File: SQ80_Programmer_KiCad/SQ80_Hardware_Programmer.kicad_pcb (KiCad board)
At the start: 2 copper layers, 225 x 115 mm, 58 parts, among them J1 MIDI IN, J2 MIDI OUT/THRU, SW1 ARCH_MODE, SW2 GLITCH_TRIG, U1 MUX_1, U2 MUX_2, U3 6N138, U4 ER_OLEDM0.91_1x-I2C

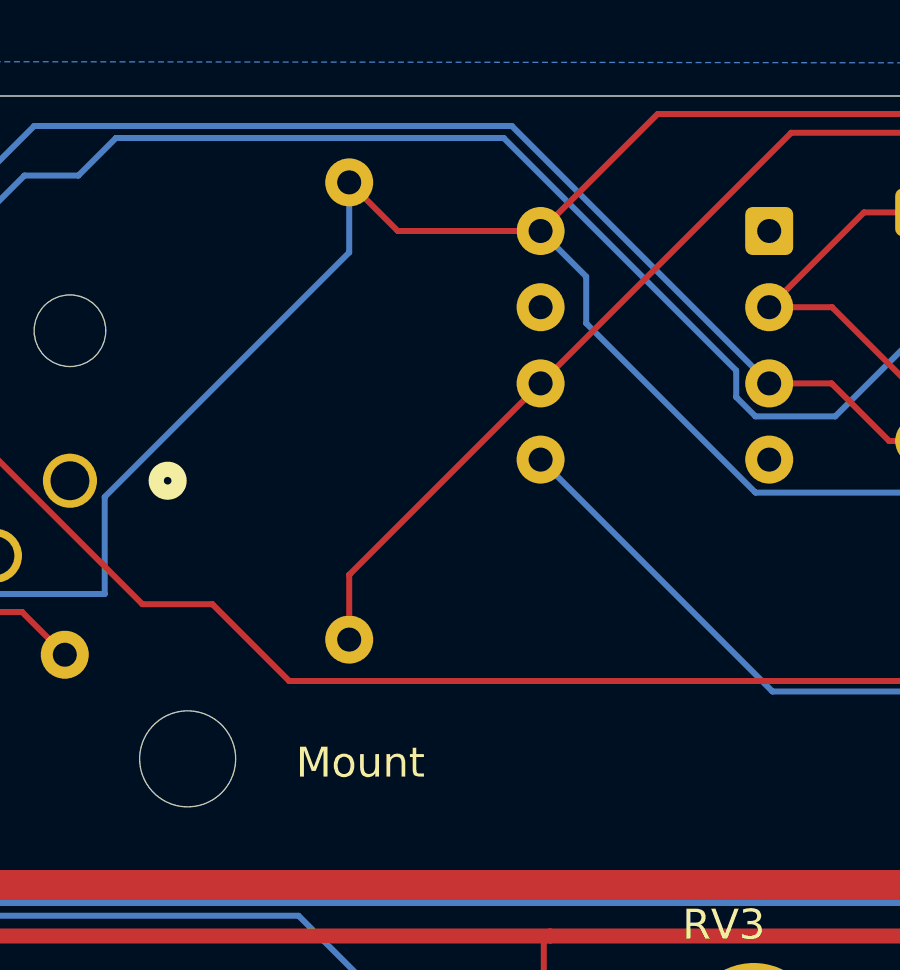
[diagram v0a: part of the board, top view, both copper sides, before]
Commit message: PCB and Readme Updates
Added functional descriptions for SW1 and SW2 in README.  Update PCB to add R5 to MIDI input section.
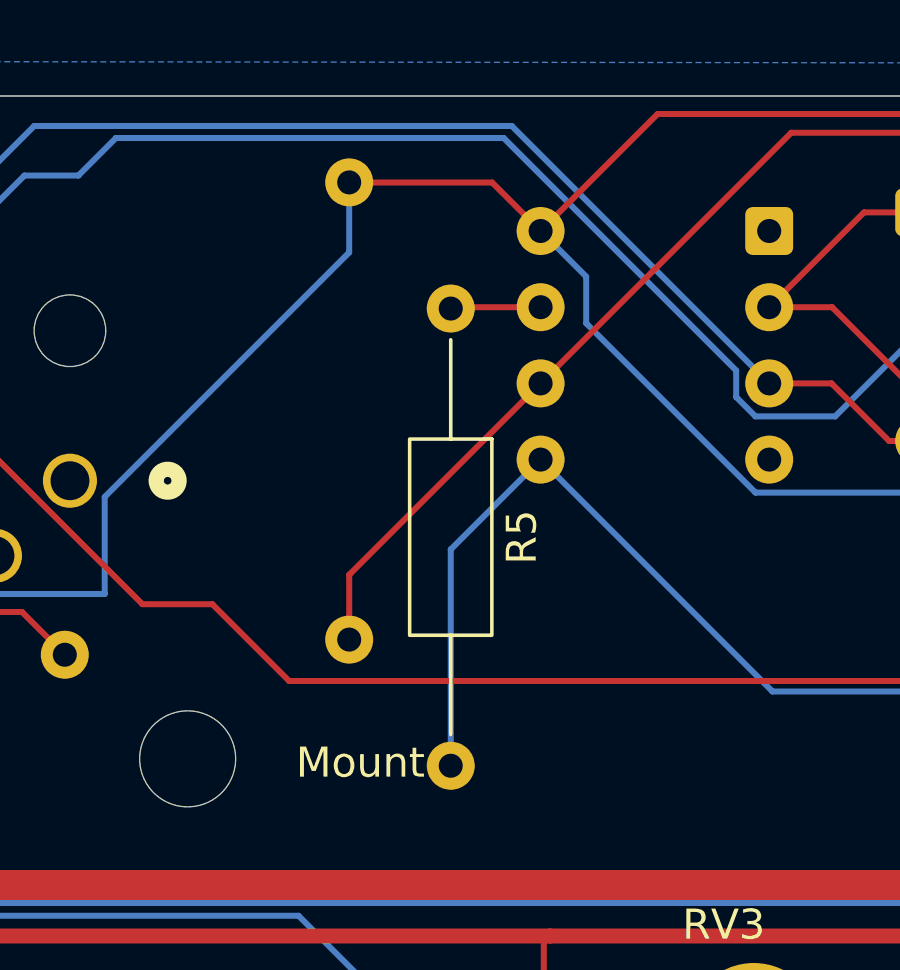
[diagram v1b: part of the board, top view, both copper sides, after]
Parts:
- added R5: 4.7k, Resistor_THT:R_Axial_DIN0207_L6.3mm_D2.5mm_P15.24mm_Horizontal, F.Cu at (96.5, 40.8)
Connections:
- U3 pad 7: unconnected-(U3-VO1-Pad7) -> Net-(U3-VO1)
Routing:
- net GND: track 1582.2 -> 1593.6 mm
- net Net-(U3-VO1): track 0.00 -> 3.01 mm
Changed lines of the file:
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@@
 		)
 	)
+	(footprint "Resistor_THT:R_Axial_DIN0207_L6.3mm_D2.5mm_P15.24mm_Horizontal"
+		(layer "F.Cu")
+		(at 96.51 40.81 -90)
+		(descr "Resistor, Axial_DIN0207 series, Axial, Horizontal, pin pitch=15.24mm, 0.25W = 1/4W, length*diameter=6.3*2.5mm^2, http://cdn-reichelt.de/documents/datenblatt/B400/1_4W%23YAG.pdf")
+		(tags "Resistor Axial_DIN0207 series Axial Horizontal pin pitch 15.24mm 0.25W = 1/4W length 6.3mm diameter 2.5mm")
+		(property "Reference" "R5"
+			(at 7.62 -2.37 90)
+			(layer "F.SilkS")
+			(effects
+				(font
+					(size 1 1)
+					(thickness 0.15)
+				)
+			)
+		)
+		(property "Value" "4.7k"
+			(at 7.62 2.37 90)
+			(layer "F.Fab")
+			(effects
+				(font
+					(size 1 1)
+					(thickness 0.15)
+				)
+			)
+		)
+		(property "Datasheet" ""
+			(at 0 0 90)
+			(layer "F.Fab")
+			(hide yes)
+			(effects
+				(font
+					(size 1.27 1.27)
+				)
+			)
+		)
+		(property "Description" "Resistor"
+			(at 0 0 90)
+			(layer "F.Fab")
+			(hide yes)
+			(effects
+				(font
+					(size 1.27 1.27)
+				)
+			)
+		)
+		(property "KiLib_Generator" "resistor/THT"
+			(at 0 0 90)
+			(layer "F.SilkS")
+			(hide yes)
+			(effects
+				(font
+					(size 1 1)
+					(thickness 0.15)
+				)
+			)
+		)
+		(property ki_fp_filters "R_*")
+		(sheetname "/")
+		(sheetfile "SQ80_Hardware_Programmer.kicad_sch")
+		(attr through_hole)
+		(duplicate_pad_numbers_are_jumpers no)
+		(fp_line
+			(start 1.04 0)
+			(end 4.35 0)
+			(stroke
+				(width 0.12)
+				(type solid)
+			)
+			(layer "F.SilkS")
+		)
+		(fp_line
+			(start 14.2 0)
+			(end 10.89 0)
+			(stroke
+				(width 0.12)
+				(type solid)
+			)
+			(layer "F.SilkS")
+		)
+		(fp_rect
+			(start 4.35 -1.37)
+			(end 10.89 1.37)
+			(stroke
+				(width 0.12)
+				(type solid)
+			)
+			(fill no)
+			(layer "F.SilkS")
+		)
+		(fp_rect
+			(start -1.05 -1.5)
+			(end 16.29 1.5)
+			(stroke
+				(width 0.05)
+				(type solid)
+			)
+			(fill no)
+			(layer "F.CrtYd")
+		)
+		(fp_line
+			(start 0 0)
+			(end 4.47 0)
+			(stroke
+				(width 0.1)
+				(type solid)
+			)
+			(layer "F.Fab")
+		)
+		(fp_line
+			(start 15.24 0)
+			(end 10.77 0)
+			(stroke
+				(width 0.1)
+				(type solid)
+			)
+			(layer "F.Fab")
+		)
+		(fp_rect
+			(start 4.47 -1.25)
+			(end 10.77 1.25)
+			(stroke
+				(width 0.1)
+				(type solid)
+			)
+			(fill no)
+			(layer "F.Fab")
+		)
+		(fp_text user "${REFERENCE}"
+			(at 7.62 0 90)
+			(layer "F.Fab")
+			(effects
+				(font
+					(size 1 1)
+					(thickness 0.15)
+				)
+			)
+		)
+		(pad "1" thru_hole circle
+			(at 0 0 270)
+			(size 1.6 1.6)
+			(drill 0.8)
+			(layers "*.Cu" "*.Mask")
+			(remove_unused_layers no)
+			(net "Net-(U3-VO1)")
+			(pintype "passive")
+		)
+		(pad "2" thru_hole circle
+			(at 15.24 0 270)
+			(size 1.6 1.6)
+			(drill 0.8)
+			(layers "*.Cu" "*.Mask")
+			(remove_unused_layers no)
+			(net "GND")
+			(pintype "passive")
+		)
+		(embedded_fonts no)
+		(model "${KICAD10_3DMODEL_DIR}/Resistor_THT.3dshapes/R_Axial_DIN0207_L6.3mm_D2.5mm_P15.24mm_Horizontal.step"
+			(offset
+				(xyz 0 0 0)
+			)
+			(scale
+				(xyz 1 1 1)
+			)
+			(rotate
+				(xyz 0 0 0)
+			)
+		)
+	)
 	(footprint "Potentiometer_THT:Potentiometer_Bourns_PTV09A-1_Single_Vertical"
 		(layer "F.Cu")
@@
 			(layers "*.Cu" "*.Mask")
 			(remove_unused_layers no)
-			(net "unconnected-(U3-VO1-Pad7)")
+			(net "Net-(U3-VO1)")
 			(pinfunction "VO1_7")
-			(pintype "passive+no_connect")
+			(pintype "passive")
 		)
 		(pad "8" thru_hole circle
@@
 	)
 	(segment
+		(start 96.51 56.05)
+		(end 96.51 48.84)
+		(width 0.2)
+		(layer "B.Cu")
+		(net "GND")
+	)
+	(segment
 		(start 239.125 106.225)
 		(end 237.8 106.225)
@@
 	)
 	(segment
+		(start 96.51 48.84)
+		(end 99.505 45.845)
+		(width 0.2)
+		(layer "B.Cu")
+		(net "GND")
+	)
+	(segment
 		(start 178.210001 56.74)
 		(end 180.750001 59.28)
@@
 	)
 	(segment
+		(start 93.13 36.61)
+		(end 93.125 36.605)
+		(width 0.2)
+		(layer "F.Cu")
+		(net "+5V")
+	)
+	(segment
 		(start 71.125 108.225)
 		(end 42.625 108.225)
@@
 	)
 	(segment
+		(start 97.89 36.61)
+		(end 93.13 36.61)
+		(width 0.2)
+		(layer "F.Cu")
+		(net "+5V")
+	)
+	(segment
 		(start 205.3 61.775)
 		(end 205.25 61.725)
@@
 	)
 	(segment
-		(start 99.505 38.225)
-		(end 94.745 38.225)
-		(width 0.2)
-		(layer "F.Cu")
-		(net "+5V")
-	)
-	(segment
 		(start 99.717857 90.058333)
 		(end 99.717857 84.817857)
@@
 	)
 	(segment
-		(start 94.745 38.225)
-		(end 93.125 36.605)
-		(width 0.2)
+		(start 185.625 61.725)
+		(end 156.925 61.725)
+		(width 0.5)
 		(layer "F.Cu")
 		(net "+5V")
 	)
 	(segment
-		(start 185.625 61.725)
-		(end 156.925 61.725)
-		(width 0.5)
+		(start 99.505 38.225)
+		(end 97.89 36.61)
+		(width 0.2)
 		(layer "F.Cu")
 		(net "+5V")
@@
 	)
 	(segment
+		(start 137.595 42.455)
+		(end 148.465 53.325)
+		(width 0.2)
+		(layer "F.Cu")
+		(net "/SCL")
+	)
+	(segment
+		(start 234.185 55.81)
+		(end 234.185 57.1)
+		(width 0.2)
+		(layer "F.Cu")
+		(net "/SCL")
+	)
+	(segment
+		(start 231.7 53.325)
+		(end 234.185 55.81)
+		(width 0.2)
+		(layer "F.Cu")
+		(net "/SCL")
+	)
+	(segment
+		(start 131.125 42.455)
+		(end 137.595 42.455)
+		(width 0.2)
+		(layer "F.Cu")
+		(net "/SCL")
+	)
+	(segment
+		(start 148.465 53.325)
+		(end 231.7 53.325)
+		(width 0.2)
+		(layer "F.Cu")
+		(net "/SCL")
+	)
+	(segment
+		(start 138.315 39.915)
+		(end 150.625 52.225)
+		(width 0.2)
+		(layer "F.Cu")
+		(net "/SDA")
+	)
+	(segment
+		(start 236.725 55.045)
+		(end 236.725 57.1)
+		(width 0.2)
+		(layer "F.Cu")
+		(net "/SDA")
+	)
+	(segment
+		(start 131.125 39.915)
+		(end 138.315 39.915)
+		(width 0.2)
+		(layer "F.Cu")
+		(net "/SDA")
+	)
+	(segment
+		(start 150.625 52.225)
+		(end 233.905 52.225)
+		(width 0.2)
+		(layer "F.Cu")
+		(net "/SDA")
+	)
+	(segment
+		(start 233.905 52.225)
+		(end 236.725 55.045)
+		(width 0.2)
+		(layer "F.Cu")
+		(net "/SDA")
+	)
+	(segment
 		(start 233.6 122.622055)
 		(end 231.797055 124.425)
@@
 	)
 	(segment
-		(start 138.315 39.915)
-		(end 150.625 52.225)
-		(width 0.2)
-		(layer "F.Cu")
-		(net "/SDA")
-	)
-	(segment
-		(start 236.725 55.045)
-		(end 236.725 57.1)
-		(width 0.2)
-		(layer "F.Cu")
-		(net "/SDA")
-	)
-	(segment
-		(start 131.125 39.915)
-		(end 138.315 39.915)
-		(width 0.2)
-		(layer "F.Cu")
-		(net "/SDA")
-	)
-	(segment
-		(start 150.625 52.225)
-		(end 233.905 52.225)
-		(width 0.2)
-		(layer "F.Cu")
-		(net "/SDA")
-	)
-	(segment
-		(start 233.905 52.225)
-		(end 236.725 55.045)
-		(width 0.2)
-		(layer "F.Cu")
-		(net "/SDA")
-	)
-	(segment
-		(start 137.595 42.455)
-		(end 148.465 53.325)
-		(width 0.2)
-		(layer "F.Cu")
-		(net "/SCL")
-	)
-	(segment
-		(start 234.185 55.81)
-		(end 234.185 57.1)
-		(width 0.2)
-		(layer "F.Cu")
-		(net "/SCL")
-	)
-	(segment
-		(start 231.7 53.325)
-		(end 234.185 55.81)
-		(width 0.2)
-		(layer "F.Cu")
-		(net "/SCL")
-	)
-	(segment
-		(start 131.125 42.455)
-		(end 137.595 42.455)
-		(width 0.2)
-		(layer "F.Cu")
-		(net "/SCL")
-	)
-	(segment
-		(start 148.465 53.325)
-		(end 231.7 53.325)
-		(width 0.2)
-		(layer "F.Cu")
-		(net "/SCL")
-	)
-	(segment
 		(start 106.025 43.760635)
 		(end 106.025 42.875)
@@
 		(net "Net-(J1-Pad4)")
 	)
+	(segment
+		(start 96.555 40.765)
+		(end 96.51 40.81)
+		(width 0.2)
+		(layer "F.Cu")
+		(net "Net-(U3-VO1)")
+	)
+	(segment
+		(start 99.505 40.765)
+		(end 96.555 40.765)
+		(width 0.2)
+		(layer "F.Cu")
+		(net "Net-(U3-VO1)")
+	)
 	(zone

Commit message: README Edits
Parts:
- R5: moved to B.Cu
- moved R4 1.19 mm to (91.9, 36.6)
- moved R5 0.51 mm to (96.0, 40.8)
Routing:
- net +5V: track 1501.8 -> 1502.4 mm
- net /MIDI_RX: track 139.5 -> 140.0 mm
